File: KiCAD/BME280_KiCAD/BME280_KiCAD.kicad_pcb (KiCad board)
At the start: 2 copper layers, 21 parts, among them Q1 2N7000, Q2 2N7000, Q3 2N7000, U1 D148K, U2 ESP32-S3-DevKitC, U3 D148K, U4 D148K

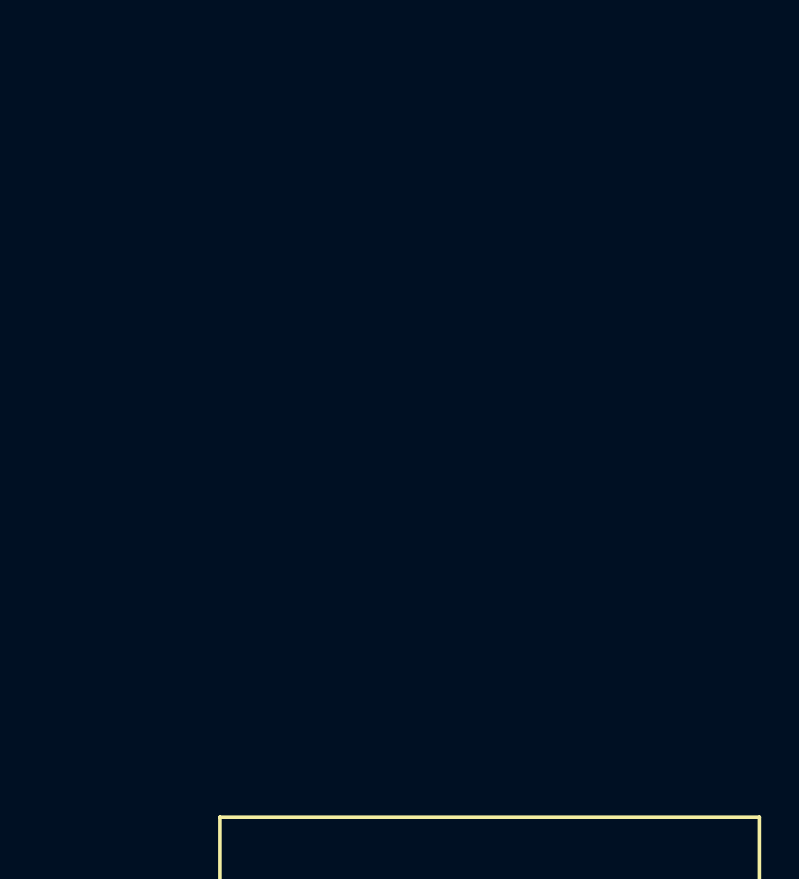
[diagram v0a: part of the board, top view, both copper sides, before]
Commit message: added code folder with a template file and the file where the full code will be.
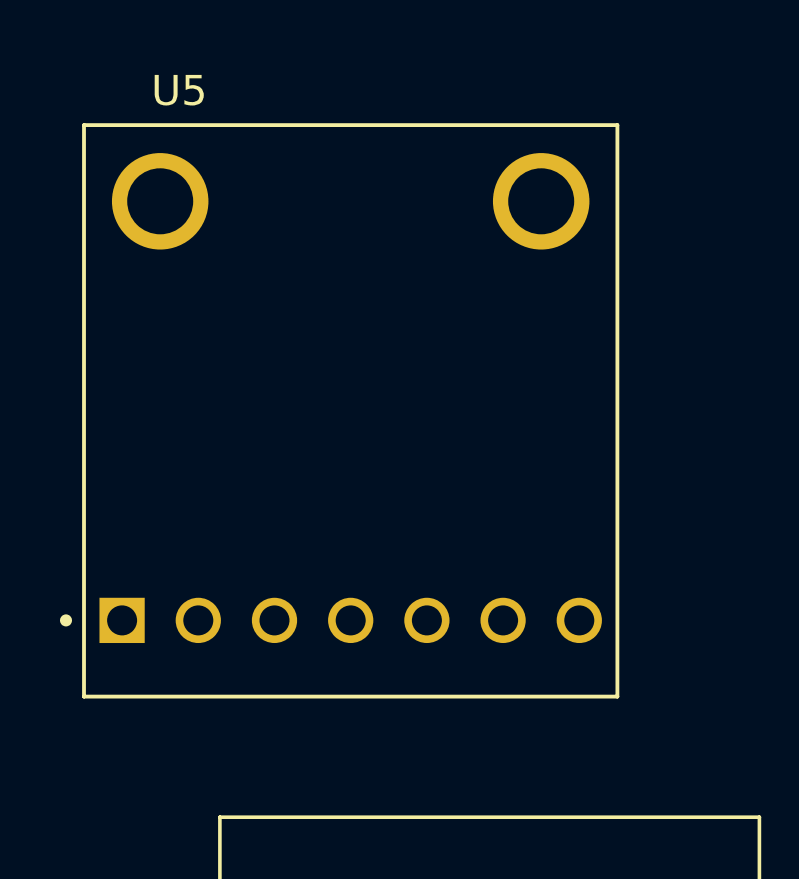
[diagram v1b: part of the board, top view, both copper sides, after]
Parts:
- added U5: 2652, BME280_local:MODULE_2652, F.Cu at (8.38, -13.5)
